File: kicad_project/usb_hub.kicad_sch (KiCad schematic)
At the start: 33 parts, among them J1 USB4105-GF-A, J2 UJ2-ADH-3-TH, U2 CY7C65632-48AXCT, U3 USBLC6-2SC6, U4 USBLC6-2SC6, U5 USBLC6-2SC6, U6 BD2221G-LBTR, U7 BD2221G-LBTR, X1 ASV-12.000MHZ-EJ-T

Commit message: More work on USB hub
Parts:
- added C18, C20: 100u, symbol Device:C_Polarized_US
- added C19, C9: 2.2u, symbol Device:C_Small
- added C21: 1u, symbol Device:C_Small
- added D1: AA3528CGSK, symbol ColorLEDs:AA3528CGSK
- added FB4, FB5: 300@100MHz, Resistor_SMD:R_1206_3216Metric, symbol Device:FerriteBead_Small
- added R1 (x2): 10k, Resistor_SMD:R_1206_3216Metric, symbol Device:R_US
- added R1: 270, Resistor_SMD:R_1206_3216Metric, symbol Device:R_US
- added R1: 100k, Resistor_SMD:R_1206_3216Metric, symbol Device:R_US
- added R1: 47k, Resistor_SMD:R_1206_3216Metric, symbol Device:R_US
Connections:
- net +3.3V: now also R1.2, R1.2, U2.37 (SELFPWR); no longer R1.1, R1.1
- net GND: now also C18.2, C19.1, C20.2, C21.1, C9.1, R1.1, R1.2, R1.2, R1.2
- net ~OVR1: now also R1.1; no longer R1.2
- net ~OVR2: now also R1.1; no longer R1.2
- net PREFILT_VBUS1: now reaches U6.5 (VOUT)
- net PREFILT_VBUS1: now also C9.2, FB4.1
- net ~CY7C65634_RESET: now reaches U2.26 (~RESET)
- net ~CY7C65634_RESET: now also C21.2, R1.1, R1.2
- net at U2.27 (TEST/I2C_SCL): now also R1.2
- net GANG/SUSPEND: now reaches U2.39 (GANG/SUSPEND)
- net GANG/SUSPEND: now also D1.2 (A), R1.1
- net VBUS1: now reaches J2.1 (VBUS1), U4.5 (VBUS)
- net VBUS1: now also C18.1, FB4.2
- net UPSTREAM_VBUS: now reaches J1.A4 (VBUS), J1.A9 (VBUS), J1.B4 (VBUS), J1.B9 (VBUS), U3.5 (VBUS)
- net UPSTREAM_VBUS: now also R1.1
- net VBUS2: now reaches J2.5 (VBUS2), U5.5 (VBUS)
- net VBUS2: now also C20.1, FB5.2
- net PREFILT_VBUS2: now reaches U7.5 (VOUT)
- net PREFILT_VBUS2: now also C19.2, FB5.1
- new net: D1.1 (K), R1.1
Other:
- note added: "External port power switches"
- moved on the sheet: C1, C14, C15, R1, U2B, U2D, U2E, U2F, U2G, U5, U6, U7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

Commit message: Finish USB hub sheet
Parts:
- removed R1: 270, Resistor_SMD:R_1206_3216Metric, symbol Device:R_US
- added D2: AA3528CGSK, ColorLEDs:AA3528, symbol ColorLEDs:AA3528CGSK
- added D3, D4: AA3528SYSK, ColorLEDs:AA3528, symbol ColorLEDs:AA3528SYSK
- added D5: AA3528SURSK, ColorLEDs:AA3528, symbol ColorLEDs:AA3528SURSK
- added R1 (x2): 270, Resistor_SMD:R_1206_3216Metric, symbol Device:R_US
- added R1 (x3): 300, Resistor_SMD:R_1206_3216Metric, symbol Device:R_US
- C1, C10, C11, C19, C2, C21, C3, C4, C5, C6, C7, C8, C9: footprint (none) -> Capacitor_SMD:C_1206_3216Metric
- C18: footprint (none) -> Capacitor_THT:CP_Radial_D8.0mm_P3.50mm; SKU (none) -> 493-6630-1-ND
- C20: footprint (none) -> Capacitor_THT:CP_Radial_D8.0mm_P3.50mm
- D1: footprint (none) -> ColorLEDs:AA3528
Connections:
- net +3.3V: now also R1.1, R1.1, R1.1
- net GANG/SUSPEND: now also D5.2 (A); no longer D1.2 (A)
- net GND: now also R1.2, R1.2, R1.2, R1.2, R1.2
- net HUB_VDD_D: no longer R1.1, R1.1, R1.1
- net GREEN2: now reaches U2.35 (GREEN[2]/SPI_MISO/FIXED_PORT2)
- net GREEN2: now also D2.2 (A)
- net AMBER2: now reaches U2.36 (AMBER[2]/SPI_MOSI/PWR_PIN_POL)
- net AMBER2: now also D4.2 (A)
- net GREEN1: now reaches U2.45 (GREEN[1]/SPI_SK/FIXED_PORT1)
- net GREEN1: now also D1.2 (A)
- net AMBER1: now reaches U2.46 (AMBER[1]/SPI_CS)
- net AMBER1: now also D3.2 (A)
- net at D1.1 (K): now also R1.1
- new net: D4.1 (K), R1.1
- new net: D5.1 (K), R1.1
- new net: D3.1 (K), R1.1
- new net: D2.1 (K), R1.1
- no-connect marks 0 -> 6
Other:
- note added: "External Ports"
- note added: "Internal Ports"
- note added: "Port Indicators"
- note added: "Upstream Port"
- moved on the sheet: R1

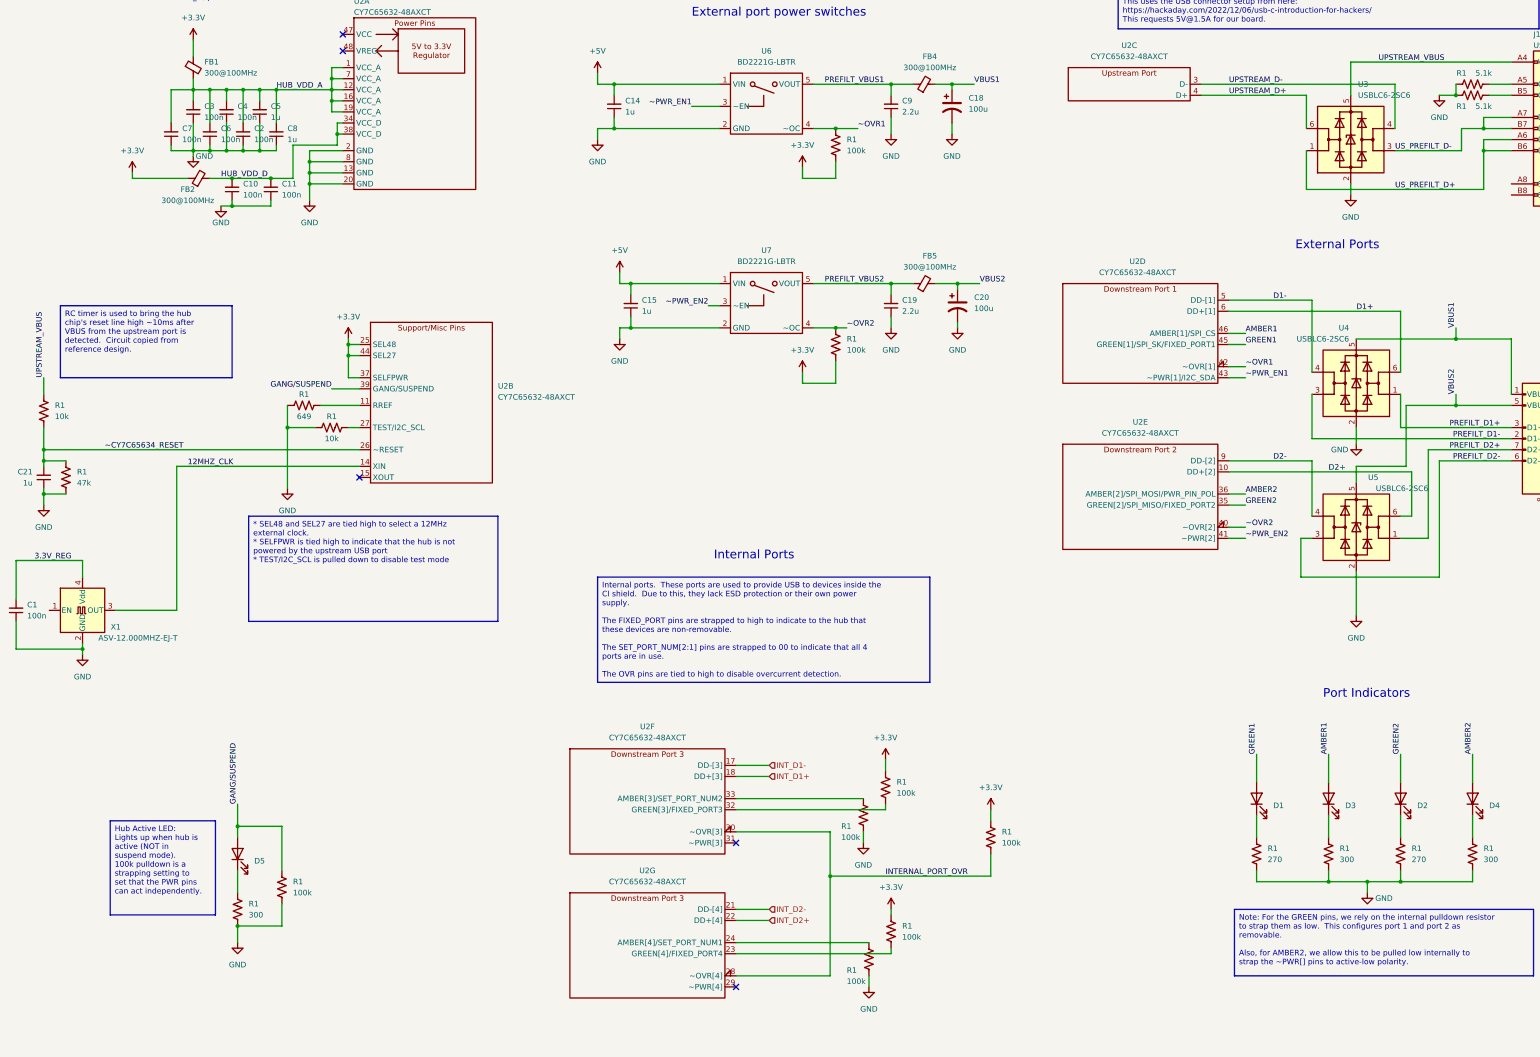
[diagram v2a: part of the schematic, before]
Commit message: Add arduino shield schematic, finish FT232H
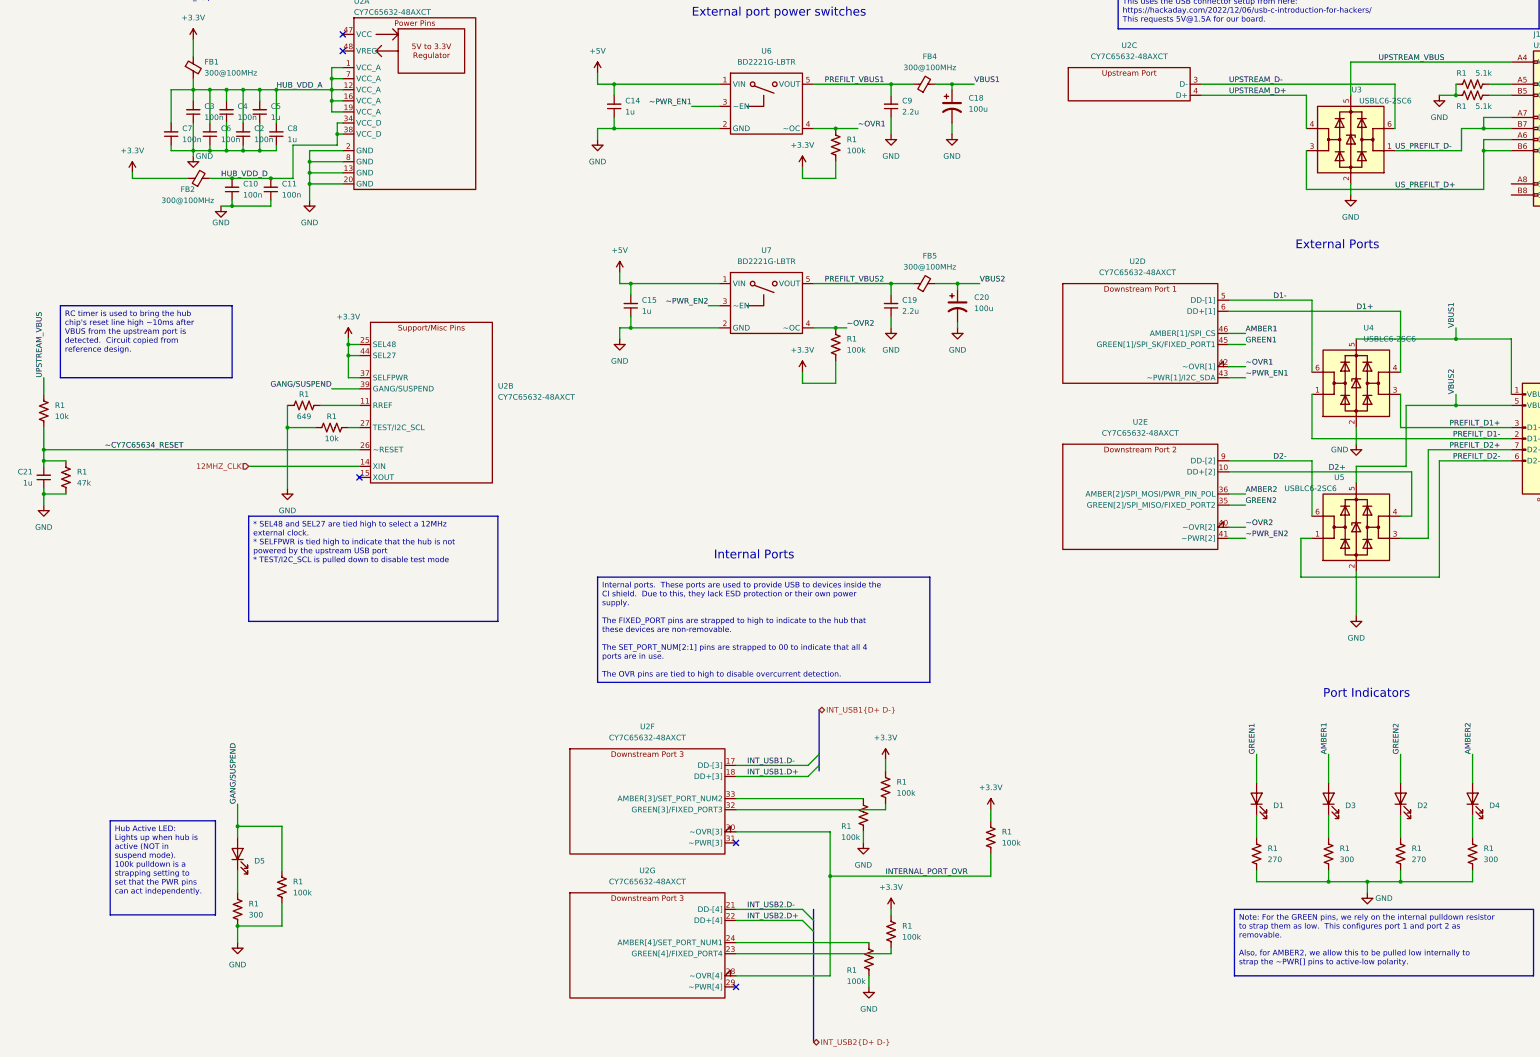
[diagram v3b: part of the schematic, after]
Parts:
- removed C1: 100n, Capacitor_SMD:C_1206_3216Metric, symbol Device:C_Small
- removed X1: ASV-12.000MHZ-EJ-T, Oscillator:Oscillator_SMD_Abracon_ASV-4Pin_7.0x5.1mm, symbol Oscillator:ASV-xxxMHz
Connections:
- net D1+: now also U4.4 (I/O2); no longer U4.6 (I/O1)
- net D1-: now also U4.6 (I/O1); no longer U4.4 (I/O2)
- net D2+: now also U5.4 (I/O2); no longer U5.6 (I/O1)
- net D2-: now also U5.6 (I/O1); no longer U5.4 (I/O2)
- net PREFILT_D1+: now also U4.3 (I/O2); no longer U4.1 (I/O1)
- net PREFILT_D1-: now also U4.1 (I/O1); no longer U4.3 (I/O2)
- net PREFILT_D2+: now also U5.3 (I/O2); no longer U5.1 (I/O1)
- net PREFILT_D2-: now also U5.1 (I/O1); no longer U5.3 (I/O2)
- net UPSTREAM_D+: now also U3.4 (I/O2); no longer U3.6 (I/O1)
- net UPSTREAM_D-: now also U3.6 (I/O1); no longer U3.4 (I/O2)
- net US_PREFILT_D+: now also U3.3 (I/O2); no longer U3.1 (I/O1)
- net US_PREFILT_D-: now also U3.1 (I/O1); no longer U3.3 (I/O2)
- net INT_D1+ renamed INT_USB1.D+
- net INT_D1- renamed INT_USB1.D-
- net INT_D2+ renamed INT_USB2.D+
- net INT_D2- renamed INT_USB2.D-

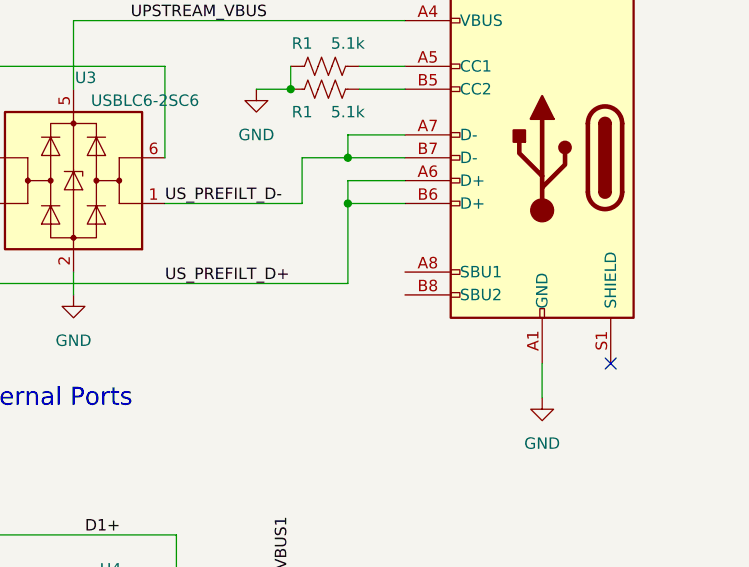
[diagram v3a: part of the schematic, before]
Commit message: Finish up initial schematic
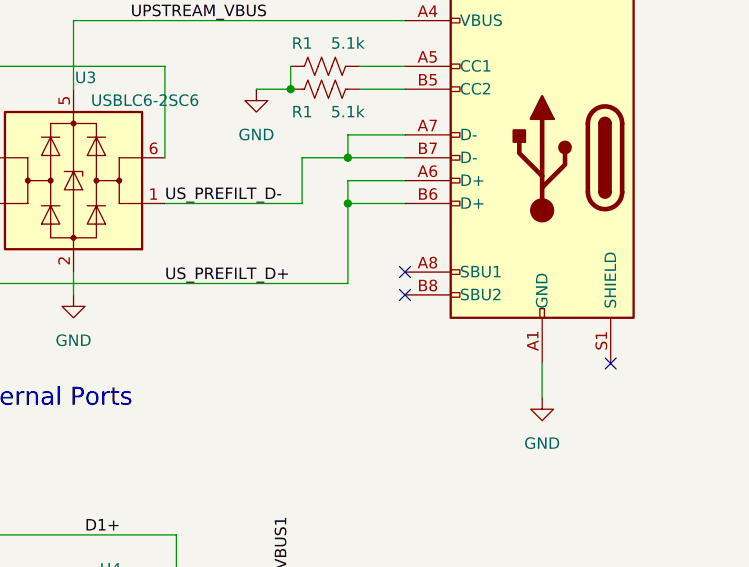
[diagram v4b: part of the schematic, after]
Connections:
- no-connect marks 6 -> 8
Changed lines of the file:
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@@
   )
   (no_connect (at 96.52 137.16))
+  (no_connect (at 360.68 69.85))
   (no_connect (at 92.71 39.37))
+  (no_connect (at 360.68 72.39))
   (no_connect (at 182.88 220.98))
   (no_connect (at 383.54 80.01))
